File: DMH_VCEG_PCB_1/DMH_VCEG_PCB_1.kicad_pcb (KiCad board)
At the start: 2 copper layers, 148 x 175 mm, 239 parts, among them J1 TS_Jack_6.35mm_Sw, J10 TS_Jack_6.35mm_Sw, J100 IDC_02x08, J11 TS_Jack_6.35mm_Sw, J12 TS_Jack_6.35mm_Sw, J13 TS_Jack_6.35mm_Sw, J14 TS_Jack_6.35mm_Sw, J15 TS_Jack_6.35mm_Sw, J16 TS_Jack_6.35mm_Sw, J17 TS_Jack_6.35mm_Sw, J18 TS_Jack_6.35mm_Sw, J19 TS_Jack_6.35mm_Sw, J2 TS_Jack_6.35mm_Sw, J20 TS_Jack_6.35mm_Sw, J200 IDC_02x08, J21 Conn_01x10_PinHeader, J22 Conn_01x10_PinHeader, J23 Conn_01x10_PinHeader, J24 Conn_01x06_PinHeader, J25 Conn_01x10_PinHeader, J26 Conn_01x10_PinHeader, J27 Conn_01x10_PinHeader, J3 TS_Jack_6.35mm_Sw, J4 TS_Jack_6.35mm_Sw, J5 TS_Jack_6.35mm_Sw, J6 TS_Jack_6.35mm_Sw, J7 TS_Jack_6.35mm_Sw, J8 TS_Jack_6.35mm_Sw, J9 TS_Jack_6.35mm_Sw, Q1 BC558, Q17 BC558, Q18 BC558, Q19 BC548, Q2 BC558, Q20 BC548, Q21 BS170, Q22 BS170, Q3 BC548, Q4 BC548, Q5 BS170, Q6 BS170, U1 TL074, U11 TL074, U12 4001, U13 40106, U15 TL074, U16 4001, U17 TL074, U2 4001, U25 4001, U3 40106, U5 TL074, U6 4001, U7 TL074

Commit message: PCB 1 placement in progress
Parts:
- C10, C11, C12, C22, C23, C24, C25, C27, C28, C29, C3, C30, C31, C4, C41, C42, C43, C44, C46, C47, C48, C5, C52, C53, C54, C55, C56, C57, C58, C59, C6, C60, C62, C63, C64, C68, C69, C70, C71, C72, C77, C78, C8, C80, C9, D12, D13, D14, D15, D16, D22, D23, D24, D25, D26, D3, D31, D32, D33, D34, D35, D4, D41, D42, D43, D44, D5, D6, D7, Q1, Q17, Q18, Q19, Q2, Q20, Q21, Q22, Q3, Q4, Q5, Q6, R1, R10, R100, R101, R102, R103, R104, R105, R106, R107, R108, R109, R110, R111, R113, R114, R115, R116, R117, R118, R119, R12, R120, R121, R122, R123, R128, R129, R13, R130, R131, R132, R133, R134, R135, R136, R137, R138, R139, R14, R140, R141, R142, R143, R144, R16, R17, R188, R189, R19, R190, R191, R192, R193, R194, R195, R196, R199, R2, R20, R201, R21, R22, R23, R24, R25, R26, R3, R31, R32, R33, R34, R35, R36, R37, R38, R39, R4, R40, R41, R42, R43, R44, R45, R46, R47, R5, R6, R7, R8, R9, R91, R92, R93, R94, R95, R96, R97, R98, R99, RV1, RV19, RV2, RV20, RV21, RV22, RV23, RV24, RV3, RV40, RV41, RV42, U1, U11, U12, U13, U15, U16, U17, U2, U25, U3, U5, U6, U7: moved to B.Cu
- moved RV2 347.7 mm to (-66.4, 108.7)
- moved RV3 345.3 mm to (-66.3, 100.4)
- moved RV21 344.0 mm to (-14.2, 91.6)
- moved R97 342.0 mm to (-35.0, 87.5)
- moved RV20 340.5 mm to (-14.1, 99.7)
- moved R96 339.5 mm to (-35.0, 91.5)
- moved R95 337.1 mm to (-35.0, 95.6)
- moved R94 335.0 mm to (-35.0, 99.7)
- moved R93 333.0 mm to (-35.0, 103.7)
- moved R91 329.5 mm to (-35.0, 111.8)
- moved D3 310.1 mm to (-24.7, 176.2)
- moved R1 309.9 mm to (-76.0, 175.9)
- moved R13 309.9 mm to (-65.2, 175.9)
- moved R25 309.9 mm to (-54.4, 175.9)
- moved Q1 309.0 mm to (-32.9, 174.7)
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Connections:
- U25 pad 1: Net-(C80-Pad1) -> Net-(C56-Pad1)
- U25 pad 11: Net-(J24D-Pin_4) -> Net-(J24C-Pin_3)
- U25 pad 12: Net-(C56-Pad1) -> Net-(C80-Pad1)
- U25 pad 3: Net-(J24C-Pin_3) -> Net-(J24D-Pin_4)
- U25 pad 5: Net-(J24C-Pin_3) -> Net-(J24D-Pin_4)
- U25 pad 6: Net-(D13-K) -> Net-(D32-K)
- U25 pad 8: Net-(J24D-Pin_4) -> Net-(J24C-Pin_3)
- U25 pad 9: Net-(D32-K) -> Net-(D13-K)
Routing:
- added copper zone on B.Cu, net GND
- added copper zone on F.Cu, net GND

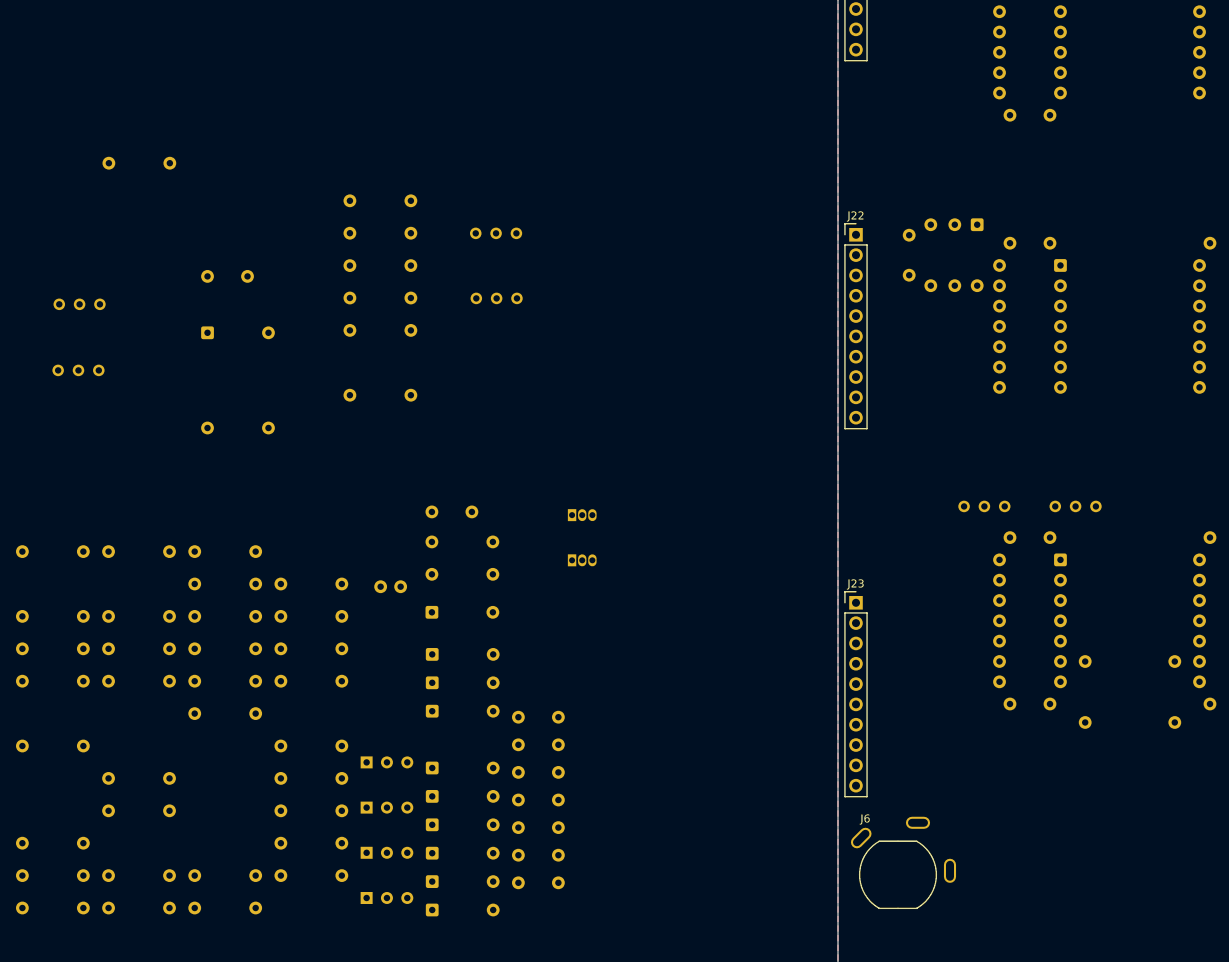
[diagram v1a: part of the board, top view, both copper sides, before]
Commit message: PCB 1 placement in progress
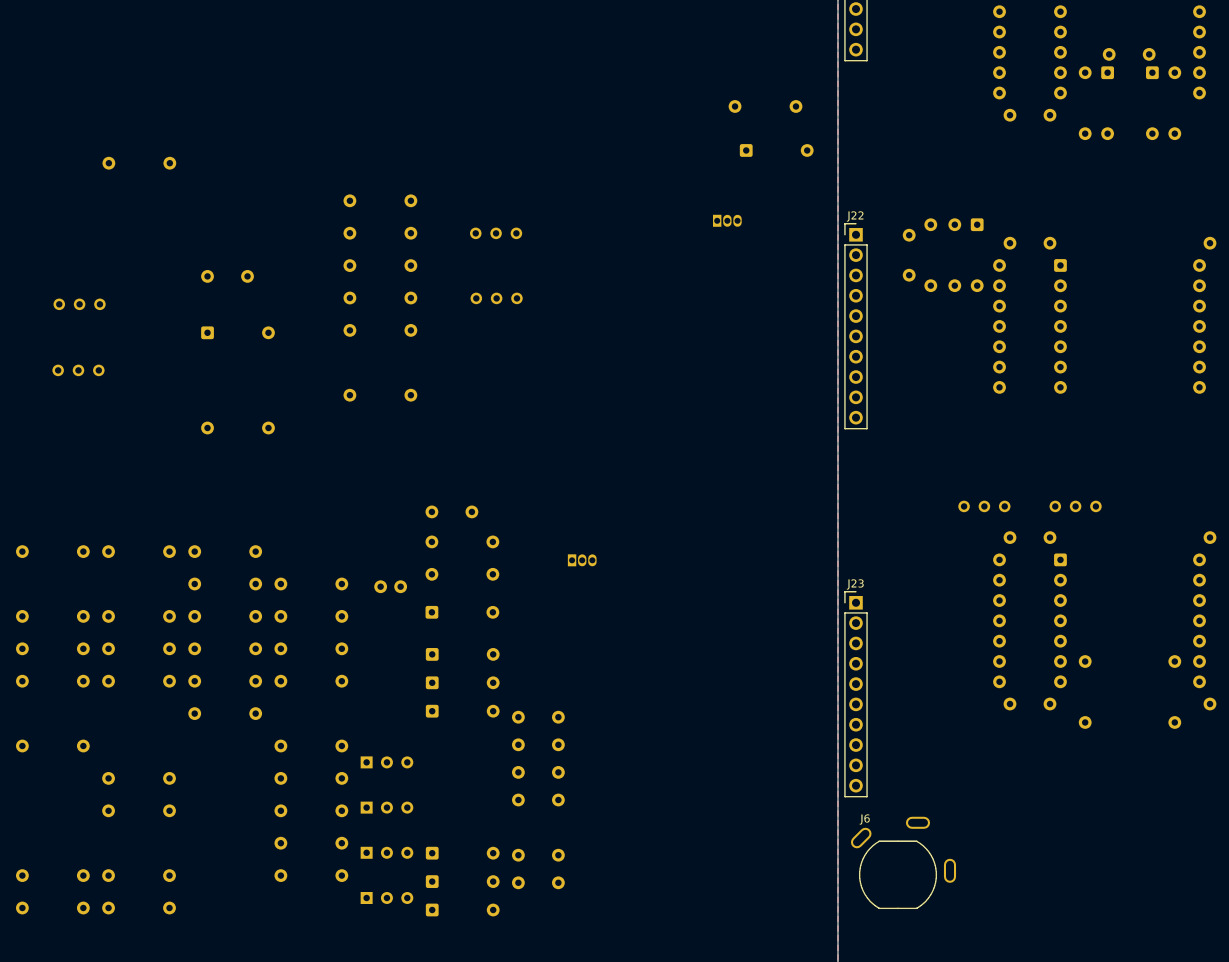
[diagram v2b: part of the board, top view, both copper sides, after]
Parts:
- moved R26 153.7 mm to (68.1, 79.1), turned to 90 degrees
- moved R25 147.5 mm to (56.9, 79.1), turned to 90 degrees
- moved D6 130.2 mm to (65.3, 71.5), turned to -90 degrees
- moved R3 128.1 mm to (13.1, 75.7)
- moved C47 124.7 mm to (64.9, 69.2), turned to 180 degrees
- moved D7 123.7 mm to (59.7, 71.5), turned to -90 degrees
- moved D12 86.6 mm to (14.5, 81.2)
- moved Q6 41.0 mm to (10.9, 90.0)

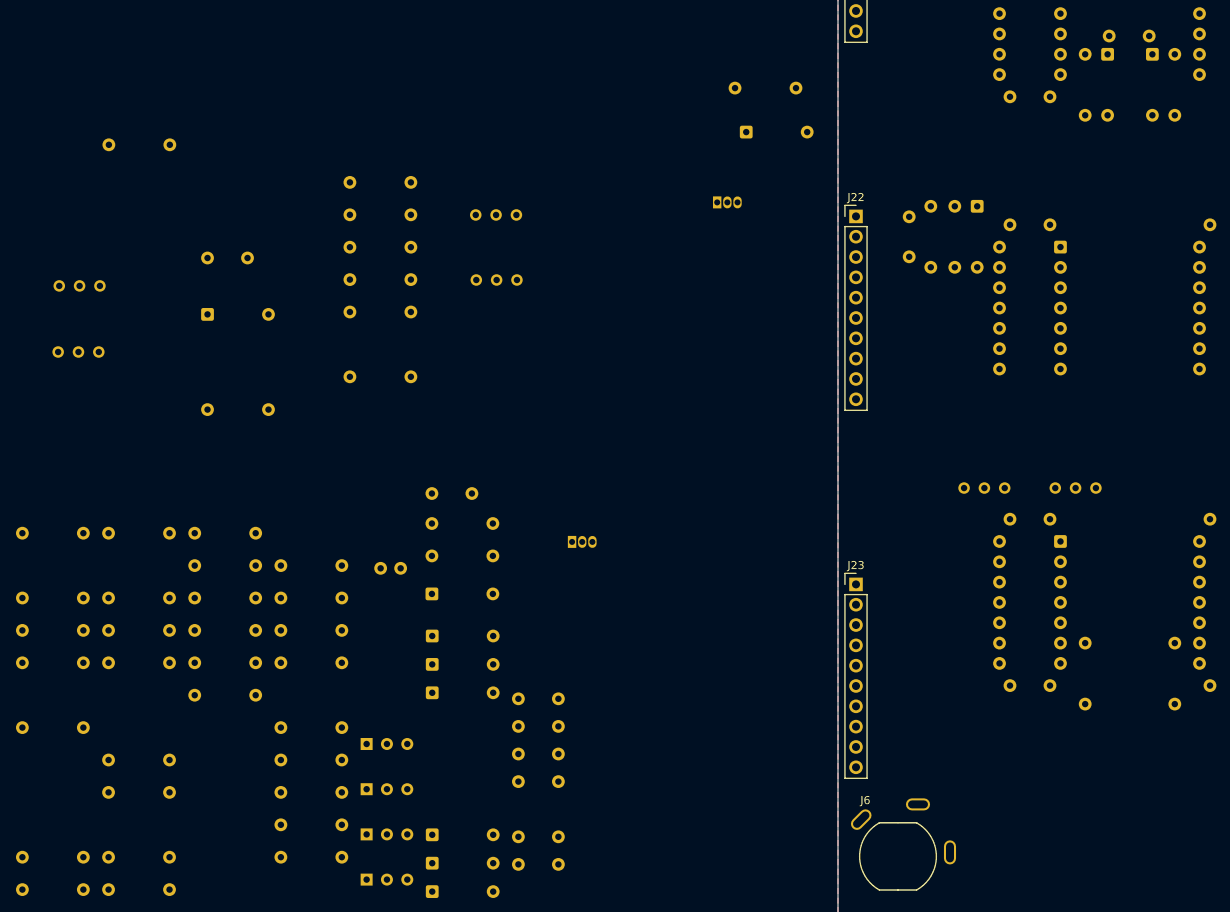
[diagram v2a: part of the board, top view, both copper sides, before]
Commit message: PCB 1 placement in progress
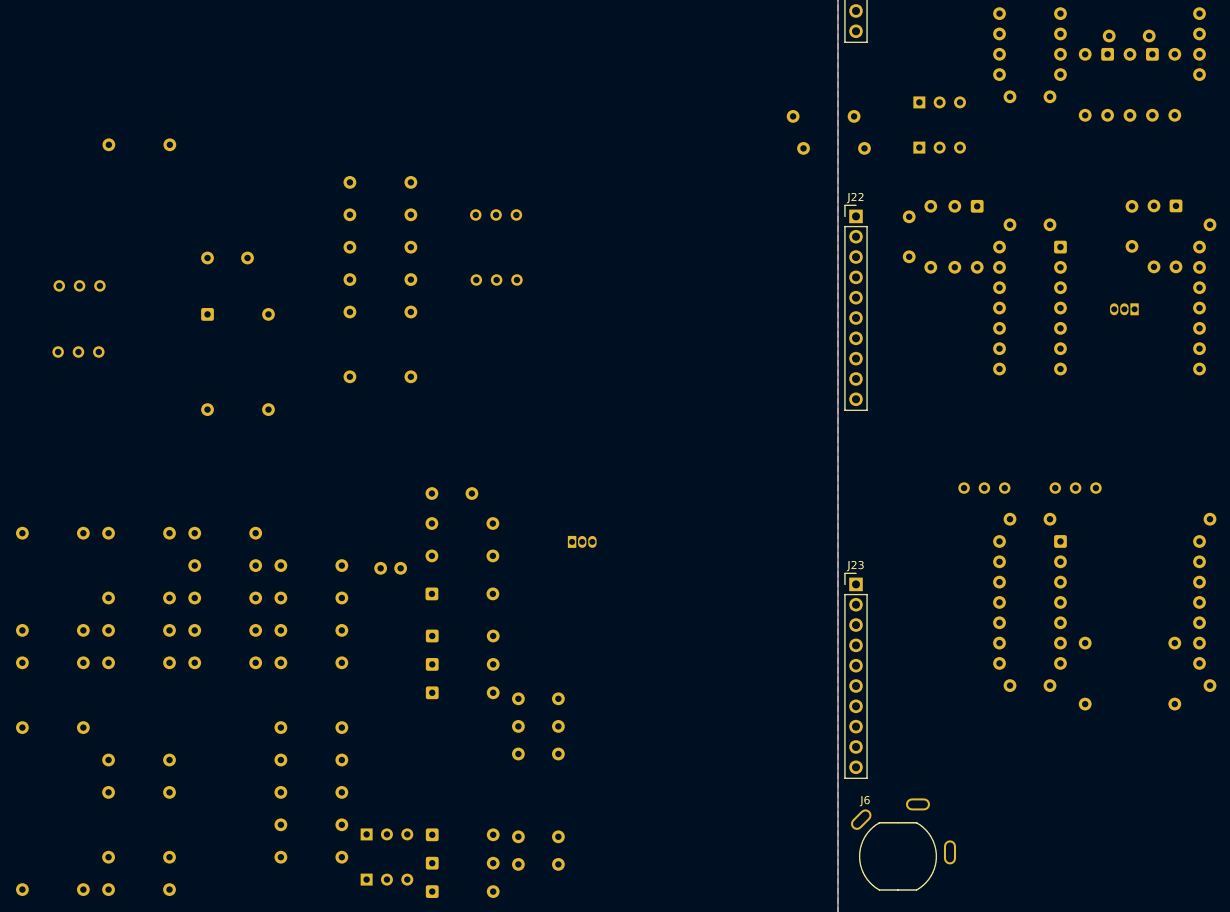
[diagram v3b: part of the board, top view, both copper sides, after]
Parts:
- moved R31 134.6 mm to (65.5, 90.4), turned to -90 degrees
- moved R2 131.8 mm to (21.7, 83.2)
- moved R10 113.6 mm to (20.4, 79.2)
- moved Q3 105.9 mm to (36.2, 83.2)
- moved Q4 105.9 mm to (36.2, 77.5)
- moved C52 105.1 mm to (62.8, 90.5), turned to -90 degrees
- moved D12 54.5 mm to (68.2, 90.4), turned to -90 degrees
- moved Q6 53.9 mm to (63.1, 103.4), turned to 180 degrees
- moved R3 49.5 mm to (62.5, 71.5), turned to -90 degrees

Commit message: PCB 1 placement in progress
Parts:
- moved R1 145.9 mm to (58.7, 119.8)
- moved R8 145.6 mm to (66.3, 116.8), turned to 180 degrees
- moved Q1 121.5 mm to (73.0, 115.2), turned to -90 degrees
- moved Q2 120.2 mm to (77.0, 120.3), turned to 90 degrees
- moved R6 108.2 mm to (29.1, 129.9)
- moved RV2 103.2 mm to (35.4, 125.7)
- moved Q5 81.4 mm to (73.7, 124.0)
- moved Q4 41.3 mm to (77.0, 83.6), turned to 90 degrees
- moved R10 38.7 mm to (58.7, 84.8)
- moved Q3 37.1 mm to (73.0, 78.5), turned to -90 degrees
- moved R2 37.0 mm to (58.7, 81.8)
- moved Q6 19.3 mm to (73.7, 87.3), turned to 0 degrees

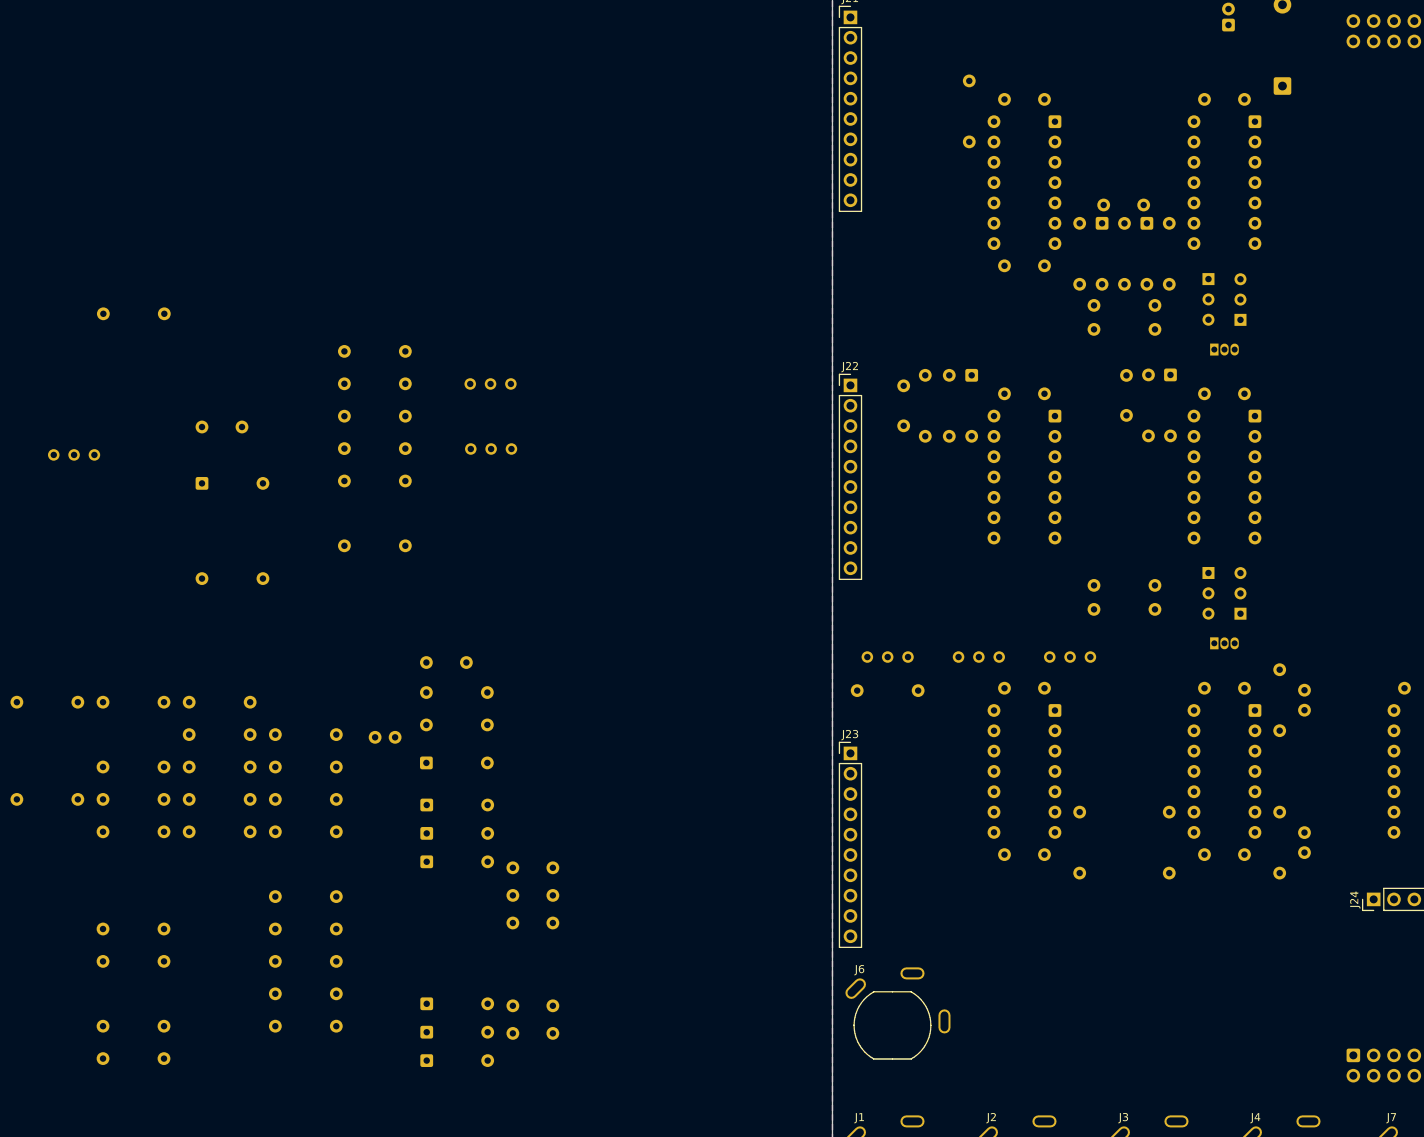
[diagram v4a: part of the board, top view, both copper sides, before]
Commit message: PCB 1 placement in progress
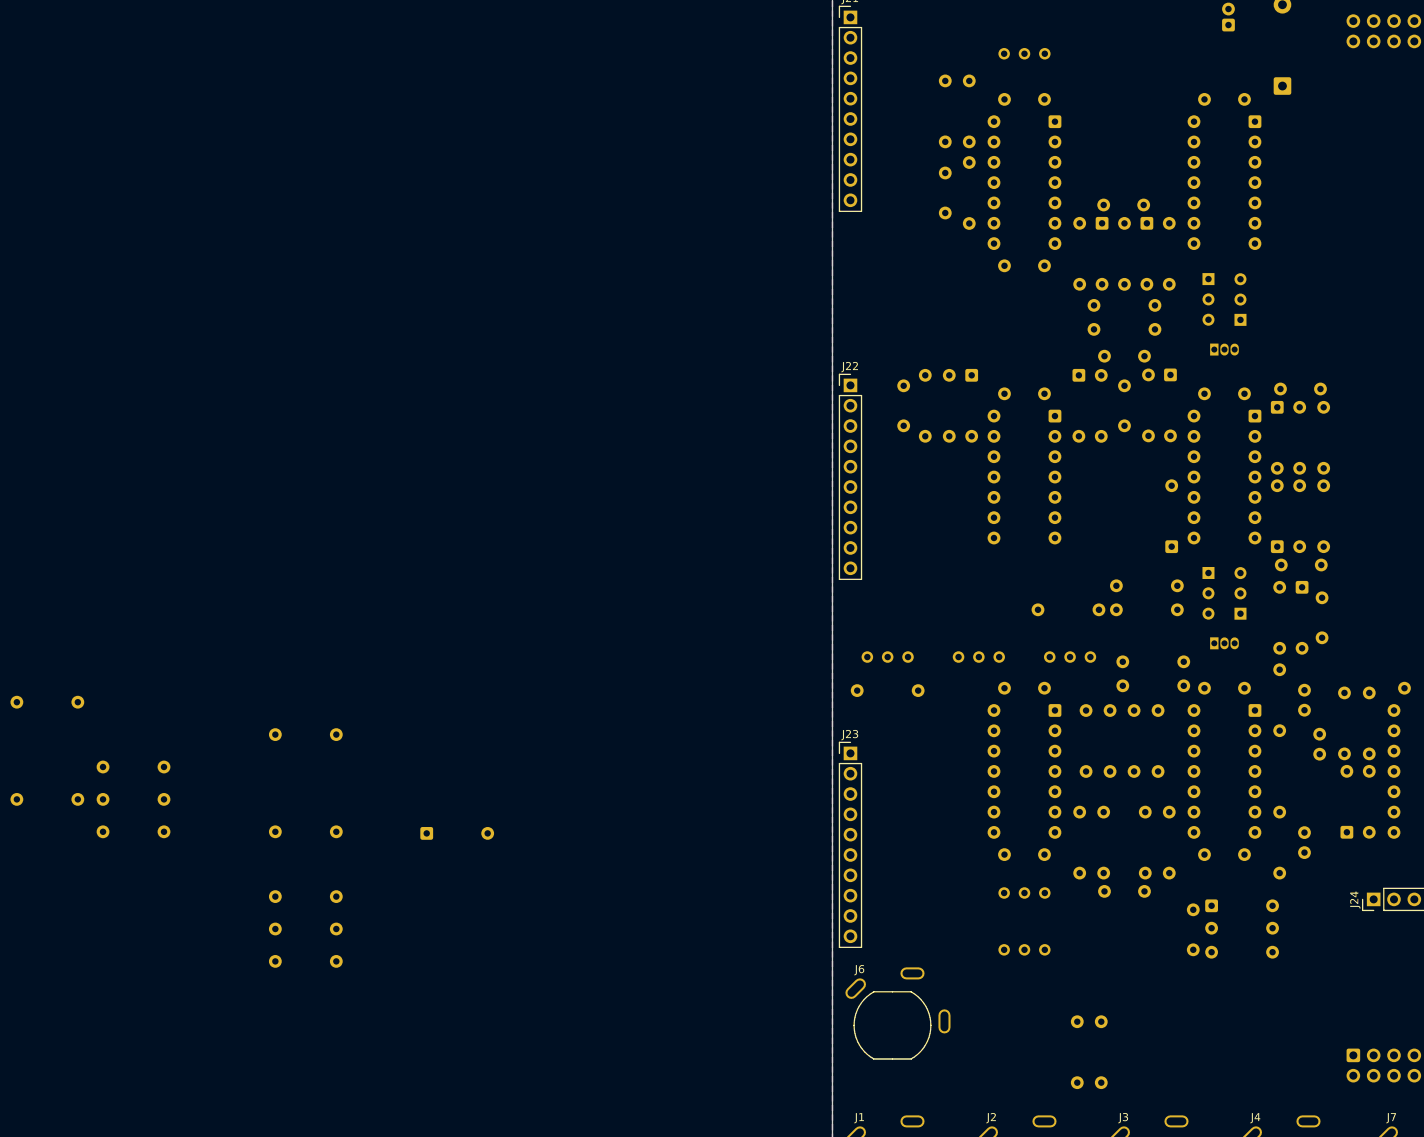
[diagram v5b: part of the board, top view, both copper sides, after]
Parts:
- moved R17 159.8 mm to (93.1, 137.8), turned to 90 degrees
- moved R16 157.3 mm to (90.0, 137.8), turned to 90 degrees
- moved R39 150.2 mm to (87.4, 94.5), turned to -90 degrees
- moved R38 149.6 mm to (84.4, 94.5), turned to -90 degrees
- moved R24 147.8 mm to (81.9, 117.0), turned to -90 degrees
- moved R32 147.7 mm to (93.1, 140.0), turned to -90 degrees
- moved R13 147.1 mm to (81.0, 159.6), turned to 180 degrees
- moved R14 146.5 mm to (81.0, 162.6), turned to 180 degrees
- moved R46 133.9 mm to (87.4, 111.9), turned to 90 degrees
- moved R45 131.9 mm to (84.4, 111.9), turned to 90 degrees
- moved RV3 124.3 mm to (47.5, 50.3), turned to 180 degrees
- moved R36 121.4 mm to (66.7, 140.0), turned to 90 degrees
- moved D5 121.2 mm to (84.7, 117.0), turned to -90 degrees
- moved D14 120.5 mm to (81.6, 94.5), turned to -90 degrees
- moved R95 118.8 mm to (56.6, 171.3), turned to -90 degrees
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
